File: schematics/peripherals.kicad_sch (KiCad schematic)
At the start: 20 parts, among them J21 PS/2, J22 port A, J23 port B, U24 CD74HCT299E, U25 CD74HCT299E, U26 SN74LS14N, U28 lcdCharScreen, U30 74HC238, X2 CXO_DIP8

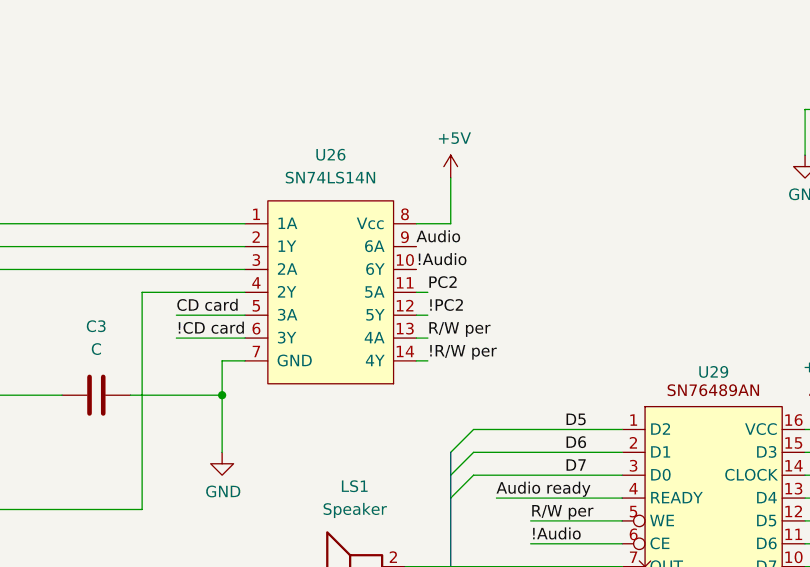
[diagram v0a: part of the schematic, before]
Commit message: Update schematics pin numbers
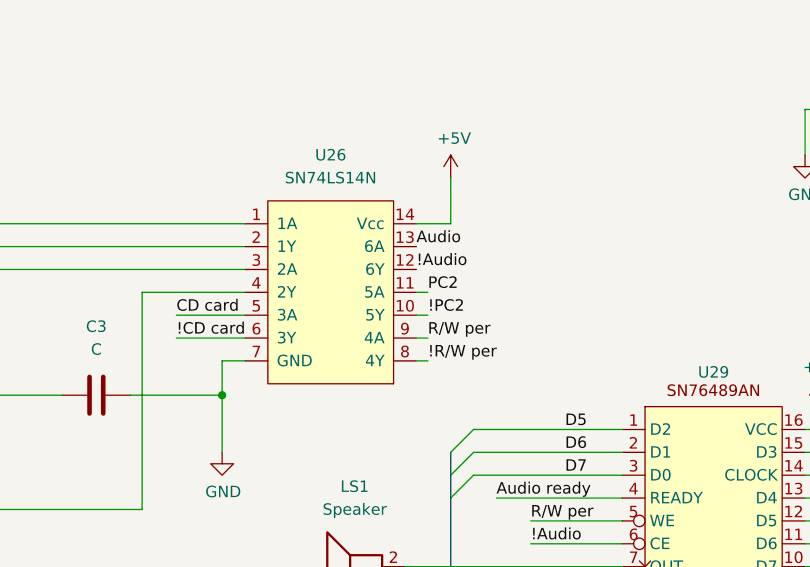
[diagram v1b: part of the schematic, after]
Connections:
- net !Audio: now also U26.12 (6Y); no longer U26.10 (6Y)
- net !PC2: now also U26.10 (5Y); no longer U26.12 (5Y)
- net !R/W per: now also U26.8 (4Y); no longer U26.14 (4Y)
- net +5V: now also U26.14 (Vcc); no longer U26.8 (Vcc)
- net Audio: now also U26.13 (6A); no longer U26.9 (6A)
- net R/W per: now also U26.9 (4A); no longer U26.13 (4A)

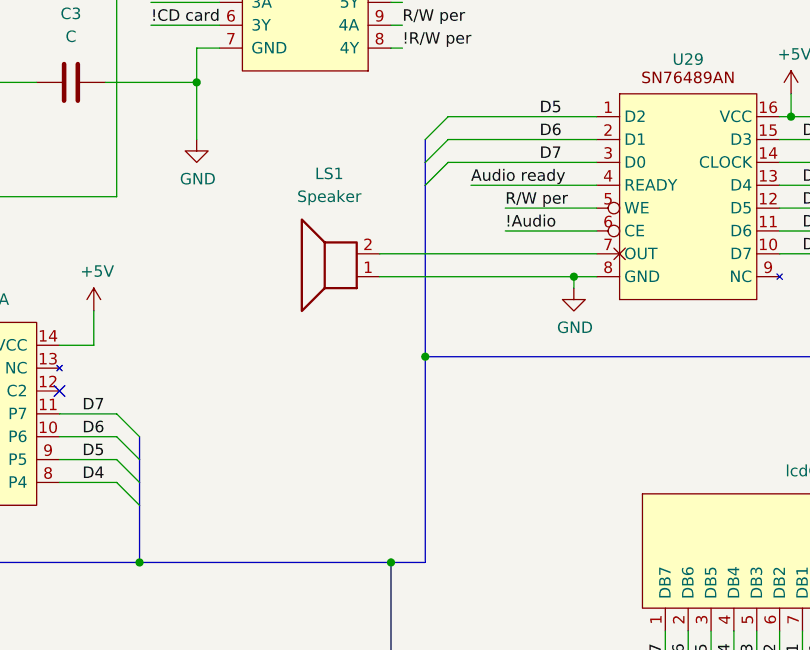
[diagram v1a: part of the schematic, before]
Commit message: Update schematics with audio amplifier
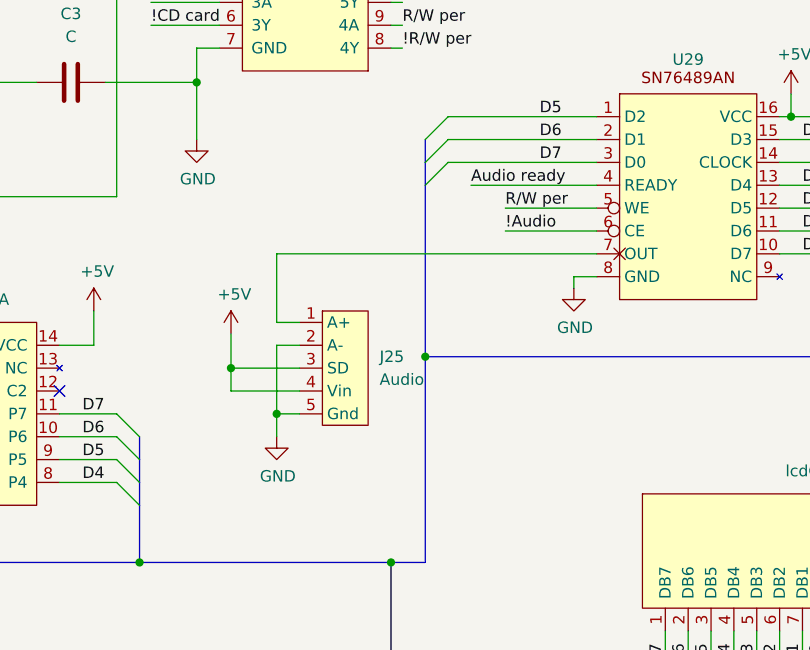
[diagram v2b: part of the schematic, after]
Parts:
- removed LS1: Speaker, symbol Device:Speaker
- added J25: Audio, symbol 6502:PAM8302A
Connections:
- net +5V: now also J25.3 (SD), J25.4 (Vin)
- net GND: now also J25.2 (A-), J25.5 (Gnd)
- net at U29.7 (OUT): now also J25.1 (A+)

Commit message: new UART support
fix schematics by adding a resistor
renaming PC/2 to correct PS/2
Updating FORTH to detect terminal connection
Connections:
- net !PC2 renamed !PS2
- net PC2 renamed PS2
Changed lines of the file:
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@@
 		)
 	)
-	(label "!PC2"
+	(label "!PS2"
 		(at 185.42 68.58 0)
 		(effects
@@
 		)
 	)
-	(label "!PC2"
+	(label "!PS2"
 		(at 48.26 58.42 0)
 		(effects
@@
 		)
 	)
-	(label "PC2"
+	(label "PS2"
 		(at 185.42 66.04 0)
 		(effects
@@
 		)
 	)
-	(label "!PC2"
+	(label "!PS2"
 		(at 48.26 106.68 0)
 		(effects
@@
 		)
 	)
-	(label "PC2"
+	(label "PS2"
 		(at 82.55 166.37 0)
 		(effects

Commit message: [ADR] 0011 autodetect peripherals
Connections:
- net at J23.6 (P2): now also J23.7 (P3)
- no-connect marks 24 -> 22

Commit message: Add resistor to clock in peripherals board
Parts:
- added R16: 68Ohm, symbol Device:R
- J24, J26, U27, U29: value ~ -> (none)
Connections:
- net PB_CLK: now reaches J24. (GND)
- net PB_CLK: now also J26.3 (CLK), R16.2
- removed net C1: J23.3 (C1), J24. (GND), J26.3 (CLK)
- new net: J23.3 (C1), R16.1
